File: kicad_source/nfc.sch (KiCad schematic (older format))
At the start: 4 parts, among them U7 M24LR

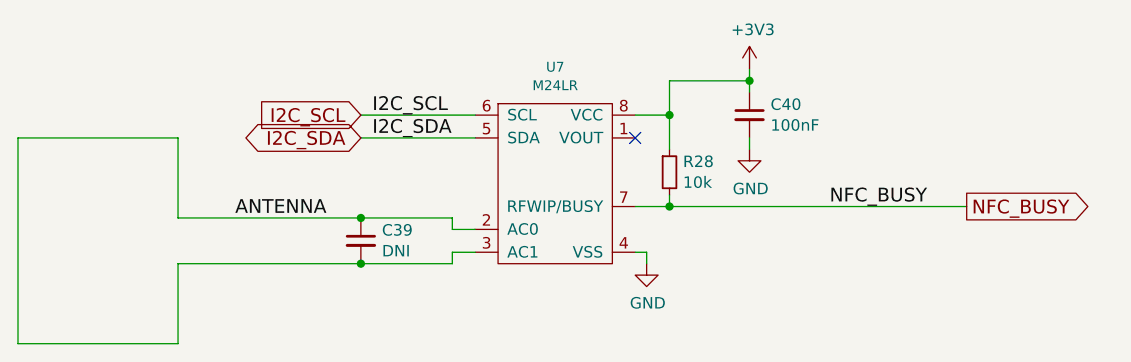
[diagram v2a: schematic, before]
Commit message: added i2c addresses to schematic pdf and readme
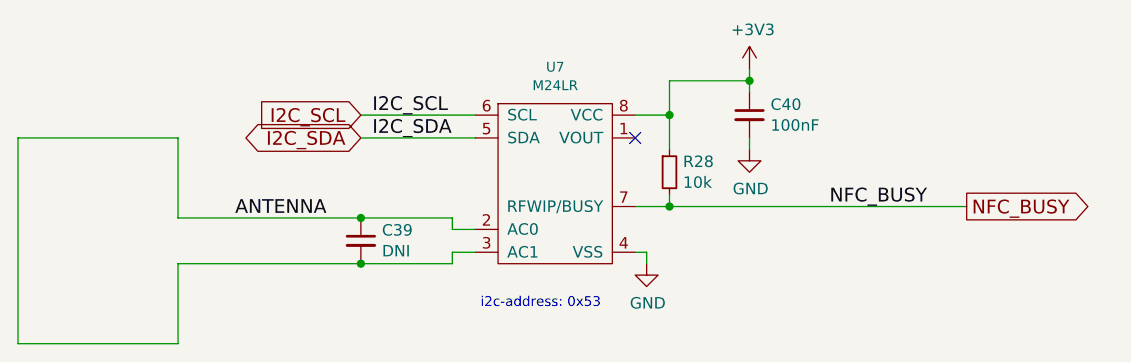
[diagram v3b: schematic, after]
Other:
- note added: "i2c-address: 0x53"
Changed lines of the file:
@@
 Sheet 6 7
 Title "NFC eeprom"
-Date "2020-07-03"
-Rev "dev_0.1"
+Date "2020-07-10"
+Rev "0.1"
 Comp "generationmake"
 Comment1 ""
@@
 Text Label 6050 3100 0    60   ~ 0
 NFC_BUSY
+Text Notes 5050 3550 2    43   ~ 0
+i2c-address: 0x53
 $EndSCHEMATC
